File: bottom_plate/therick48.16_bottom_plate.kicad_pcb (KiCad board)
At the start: 2 copper layers, 310.5 x 76 mm, 88 parts, among them U1 HOLE, U10 HOLE, U11 HOLE, U12 HOLE, U13 HOLE, U14 HOLE, U15 HOLE, U16 HOLE, U17 HOLE, U18 HOLE, U19 HOLE, U2 HOLE, U20 HOLE, U21 HOLE, U22 HOLE, U23 HOLE, U24 HOLE, U25 HOLE, U26 HOLE, U27 HOLE, U28 HOLE, U29 HOLE, U3 HOLE, U30 HOLE, U31 HOLE, U32 HOLE, U33 HOLE, U34 HOLE, U35 HOLE, U36 HOLE, U37 HOLE, U38 HOLE, U39 HOLE, U4 HOLE, U40 HOLE, U41 HOLE, U42 HOLE, U43 HOLE, U44 HOLE, U45 HOLE, U46 HOLE, U47 HOLE, U48 HOLE, U49 HOLE, U5 HOLE, U50 HOLE, U51 HOLE, U52 HOLE, U53 HOLE, U54 HOLE, U55 HOLE, U56 HOLE, U57 HOLE, U58 HOLE, U59 HOLE, U6 HOLE, U60 HOLE, U61 HOLE, U62 HOLE, U63 HOLE, U64 HOLE, U65 HOLE, U66 HOLE, U67 HOLE, U68 HOLE, U69 HOLE, U7 HOLE, U70 HOLE, U8 HOLE, U9 HOLE

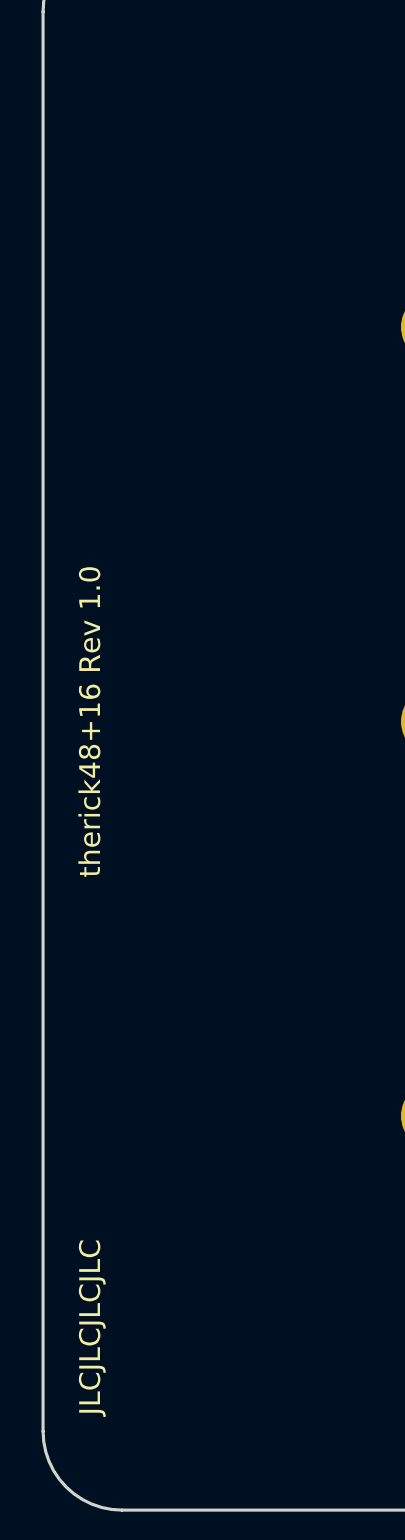
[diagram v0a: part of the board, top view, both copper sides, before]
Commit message: 48+16 to 48.16
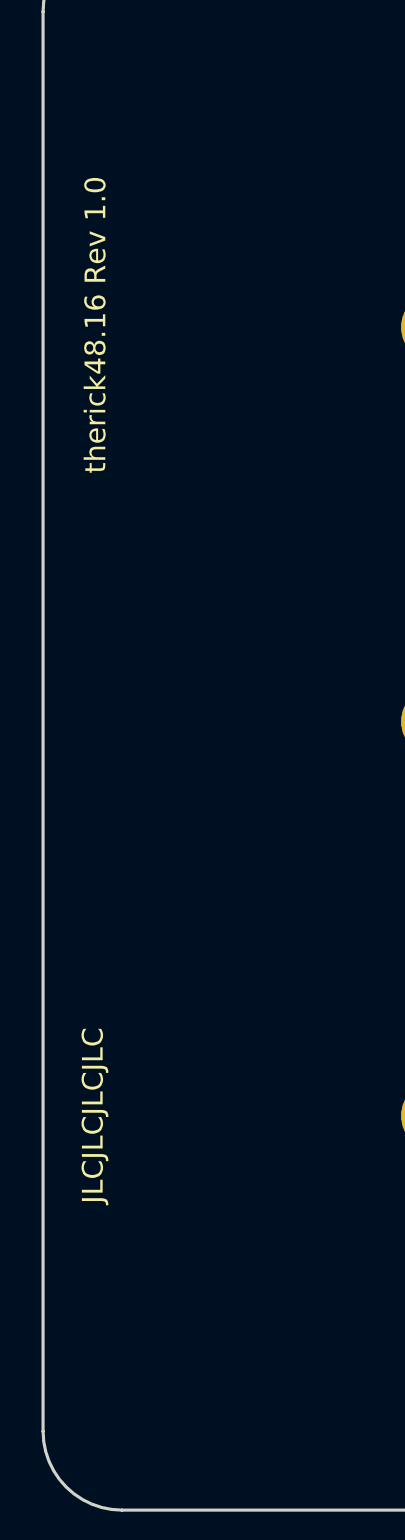
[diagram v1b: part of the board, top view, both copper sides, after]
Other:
- board text added: "therick48.16 Rev 1.0"
- board text removed: "therick48+16 Rev 1.0"
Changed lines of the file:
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@@
     (arrow2b (pts (xy 274.4104 29.26) (xy 275.536904 28.673579)))
   )
-  (gr_text "therick48+16 Rev 1.0" (at 48.639872 72.959808 90) (layer F.SilkS)
+  (gr_text "therick48.16 Rev 1.0" (at 48.895 53.848 90) (layer F.SilkS)
     (effects (font (size 1 1) (thickness 0.15)))
   )
@@
   (gr_arc (start 50.16 107.16) (end 46.36 107.16) (angle -90) (layer Edge.Cuts) (width 0.15))
   (gr_arc (start 50.16 38.76) (end 50.16 34.96) (angle -90) (layer Edge.Cuts) (width 0.15))
-  (gr_text JLCJLCJLCJLC (at 48.64 106.4 90) (layer F.SilkS)
-    (effects (font (size 1 1) (thickness 0.15)) (justify left))
+  (gr_text JLCJLCJLCJLC (at 48.768 91.948 90) (layer F.SilkS)
+    (effects (font (size 1 1) (thickness 0.15)))
   )
   (gr_line (start 217.4875 89.69375) (end 217.4875 94.45625) (layer Dwgs.User) (width 0.15))
